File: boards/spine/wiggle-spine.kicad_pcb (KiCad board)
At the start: 2 copper layers, 114.3 x 88.9 mm, 187 parts, among them CON1 USB-B, CON2 XLR-3 Female, CON3 USB-A, CON4 2.5mm 5-24V 5A, CON5 5-24V 16A, CON6 PLR135, CON7 PLT133, Q1 DMN3190LDW, Q2 2N7002P, Q3 AOD4189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

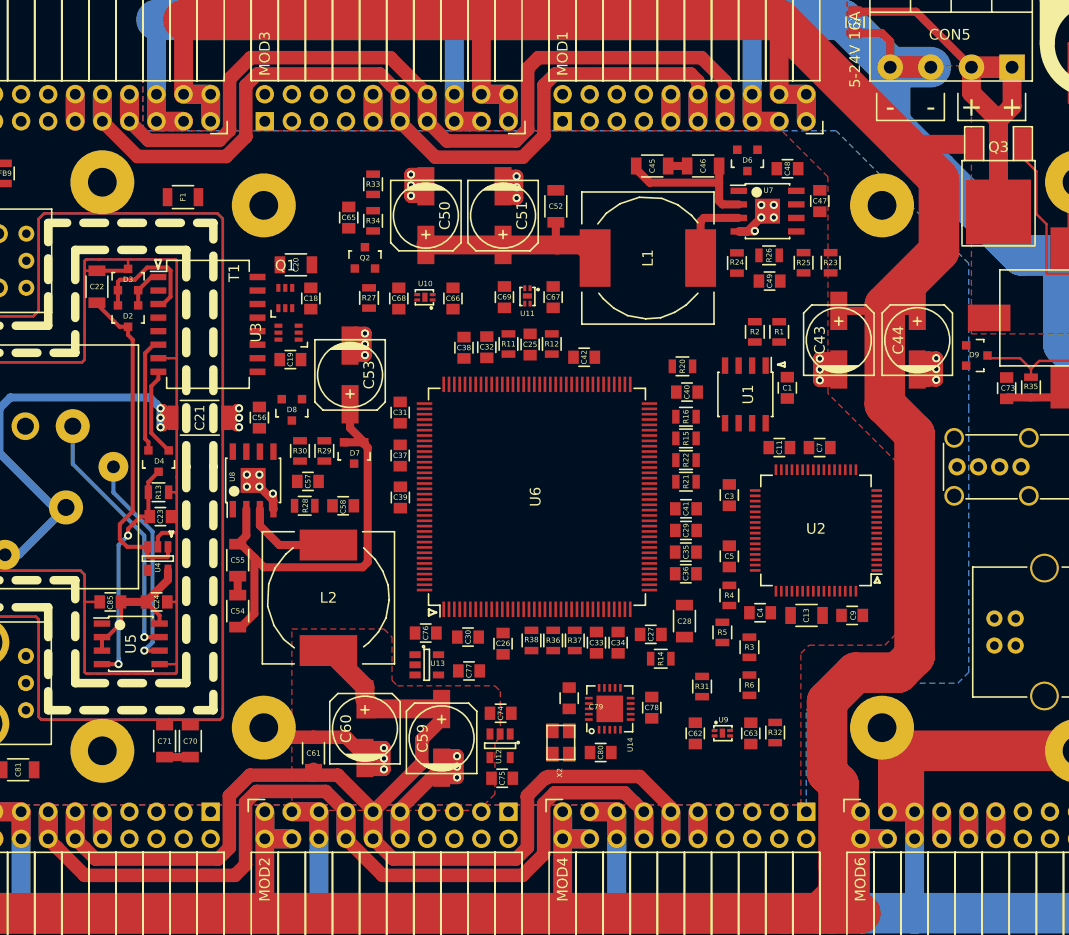
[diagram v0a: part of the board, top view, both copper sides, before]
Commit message: GND distribution, DMX via tweaks
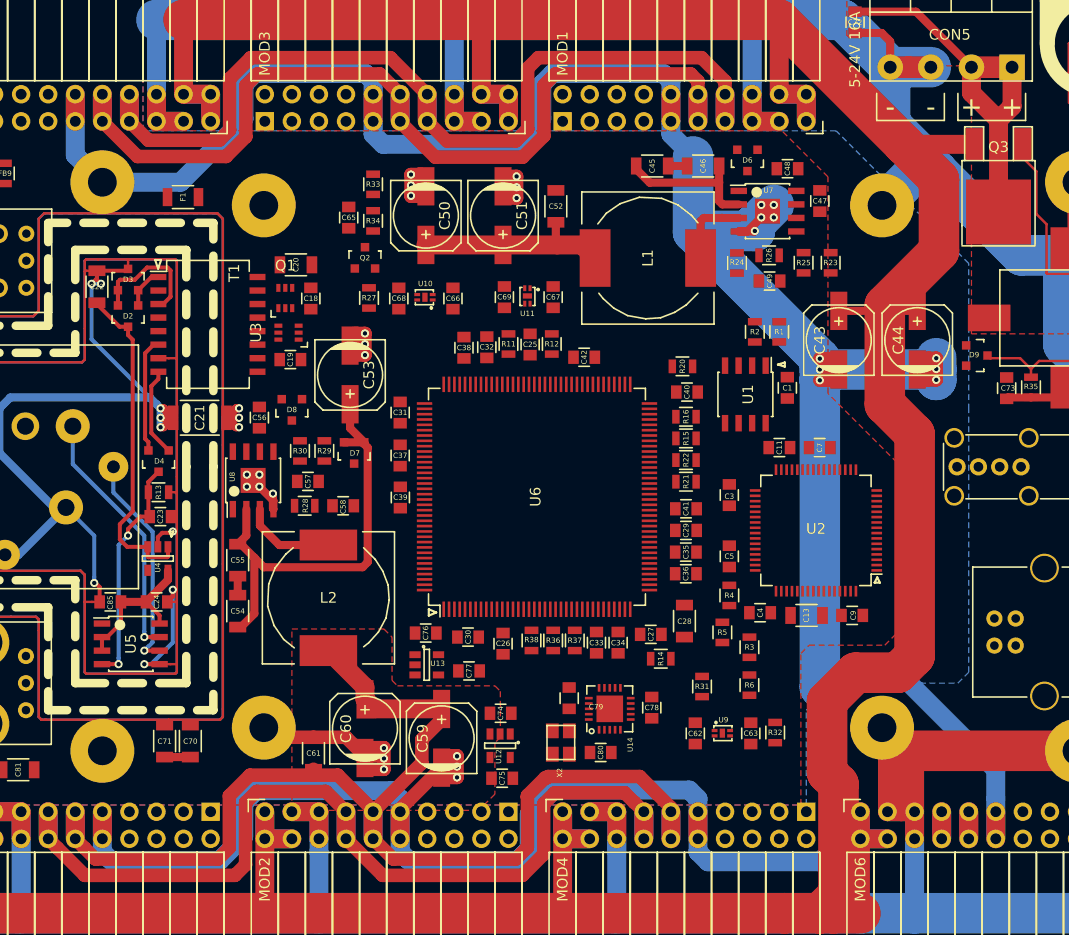
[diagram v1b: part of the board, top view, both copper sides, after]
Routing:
- net GND: track 365.1 -> 681.7 mm
- net /DMX512/DMXGND: track 269.8 -> 308.7 mm, vias 3 -> 9
- net GNDPWR: track 508.3 -> 514.8 mm

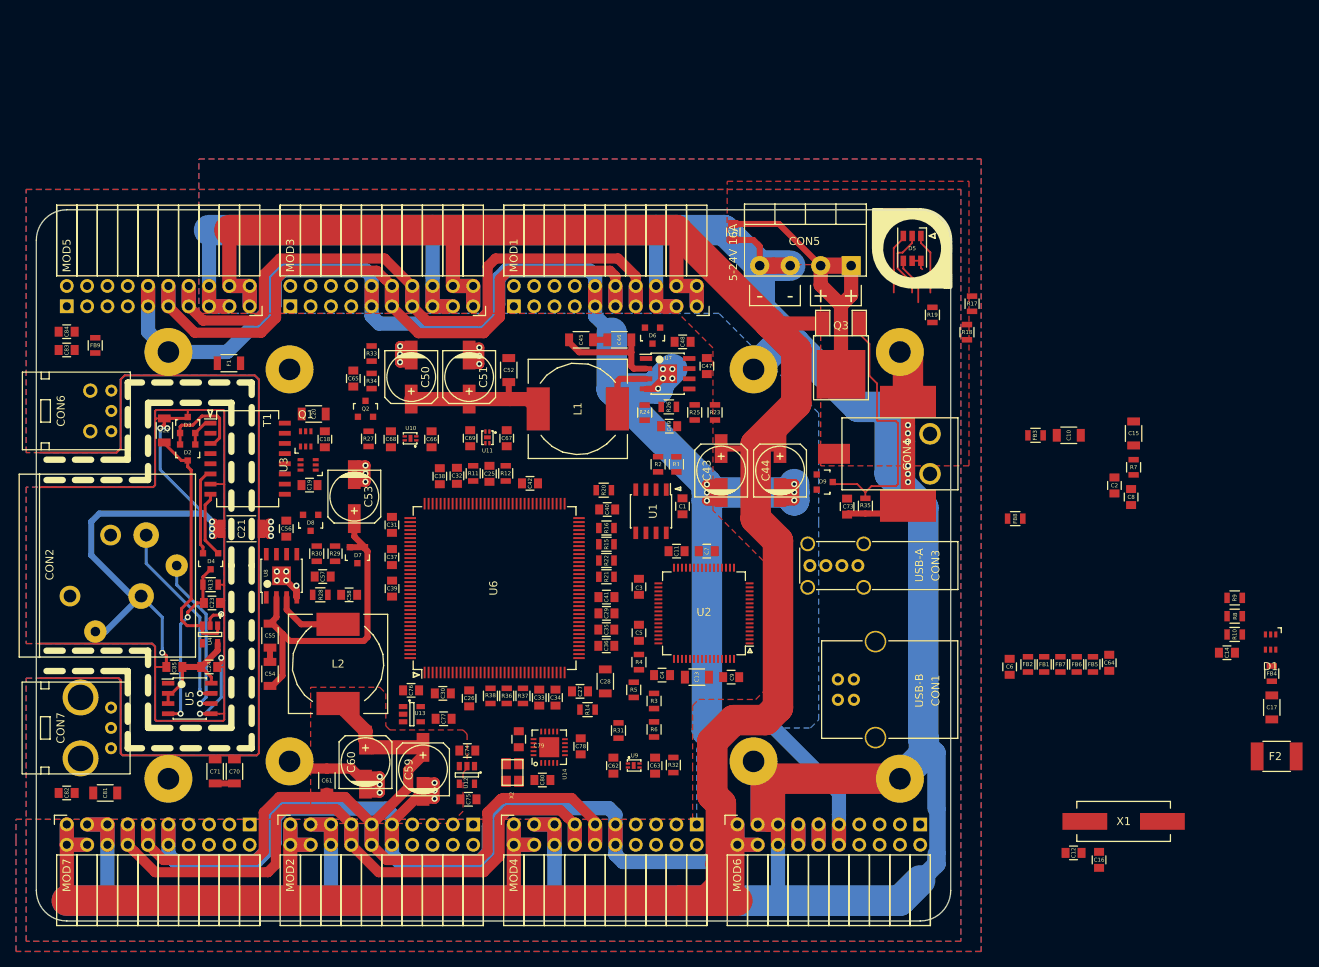
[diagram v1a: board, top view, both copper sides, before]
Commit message: Feeling better about GNDPWR and GND along the edges
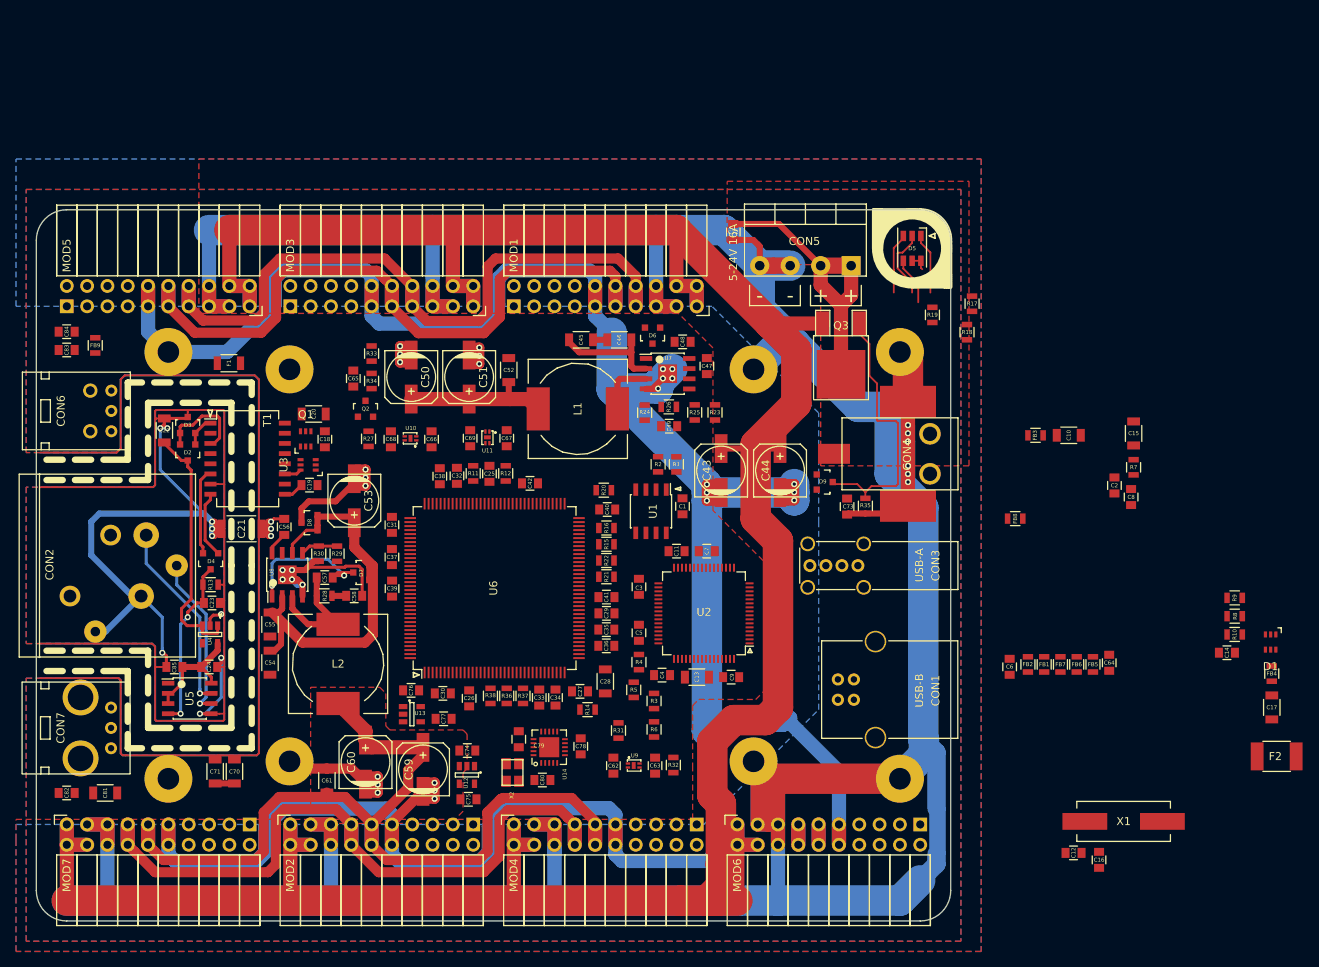
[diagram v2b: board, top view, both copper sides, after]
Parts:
- moved D7 2.21 mm to (125.7, 87.2), turned to 90 degrees
- moved C55 1.40 mm to (114.3, 93.8)
- moved C54 1.40 mm to (114.3, 98.5), turned to 270 degrees
- moved U8 0.73 mm to (116.5, 87.5)
- moved C58 0.65 mm to (124.8, 90.2)
- moved R28 0.52 mm to (121.1, 90.2)
- moved C53 0.51 mm to (124.8, 78.3)
- moved C56 0.34 mm to (116.1, 81.5), turned to 90 degrees
- moved C57 0.28 mm to (121.1, 87.9)
- moved R29 0.25 mm to (122.7, 84.9)
- moved R30 0.25 mm to (120.4, 84.9)
- moved D8 0.15 mm to (119.2, 81.0), turned to 90 degrees
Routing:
- net GND: track 681.7 -> 713.9 mm
- net Net-(C57-Pad2): track 0.00 -> 18.6 mm, vias 0 -> 2
- net +5V: track 228.3 -> 245.7 mm
- net Net-(C57-Pad1): track 8.72 -> 15.0 mm
- net Net-(R29-Pad1): track 0.00 -> 4.69 mm
- net Net-(C56-Pad1): track 0.00 -> 2.92 mm
- net Net-(C19-Pad1): track 0.00 -> 2.55 mm
- net Net-(T1-Pad11): track 0.00 -> 2.16 mm
- net Net-(C58-Pad2): track 0.00 -> 1.78 mm

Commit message: Wiggle through the thick verticals
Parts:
- moved R29 4.14 mm to (119.6, 82.2), turned to 180 degrees
- moved D7 3.61 mm to (122.9, 85.0)
- moved D8 1.89 mm to (119.3, 79.1), turned to 0 degrees
- moved C58 1.15 mm to (124.0, 89.4), turned to 270 degrees
- moved R27 0.95 mm to (126.6, 69.6), turned to 0 degrees
- moved R30 0.25 mm to (120.1, 84.9)
- moved R28 0.25 mm to (120.8, 90.2)
- moved U8 0.13 mm to (116.3, 87.5)
- moved C57 0.11 mm to (121.0, 87.9)
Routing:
- net +3V3: track 213.1 -> 332.6 mm
- net +5V: track 245.7 -> 292.5 mm
- net GND: track 713.9 -> 752.6 mm, vias 34 -> 37
- net Net-(C57-Pad2): track 18.6 -> 11.7 mm, vias 2 -> 1
- net GNDPWR: track 514.8 -> 509.8 mm

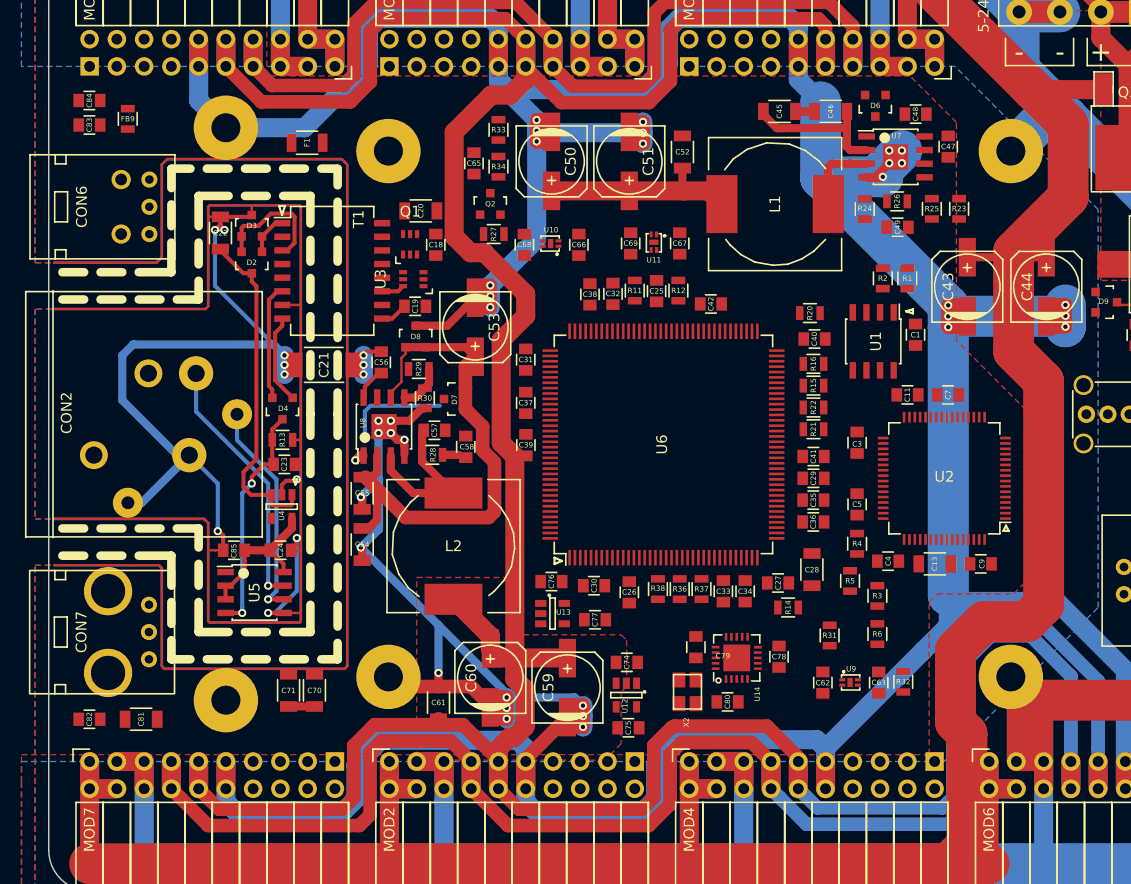
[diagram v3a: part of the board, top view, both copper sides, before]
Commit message: Lots more thick power routing
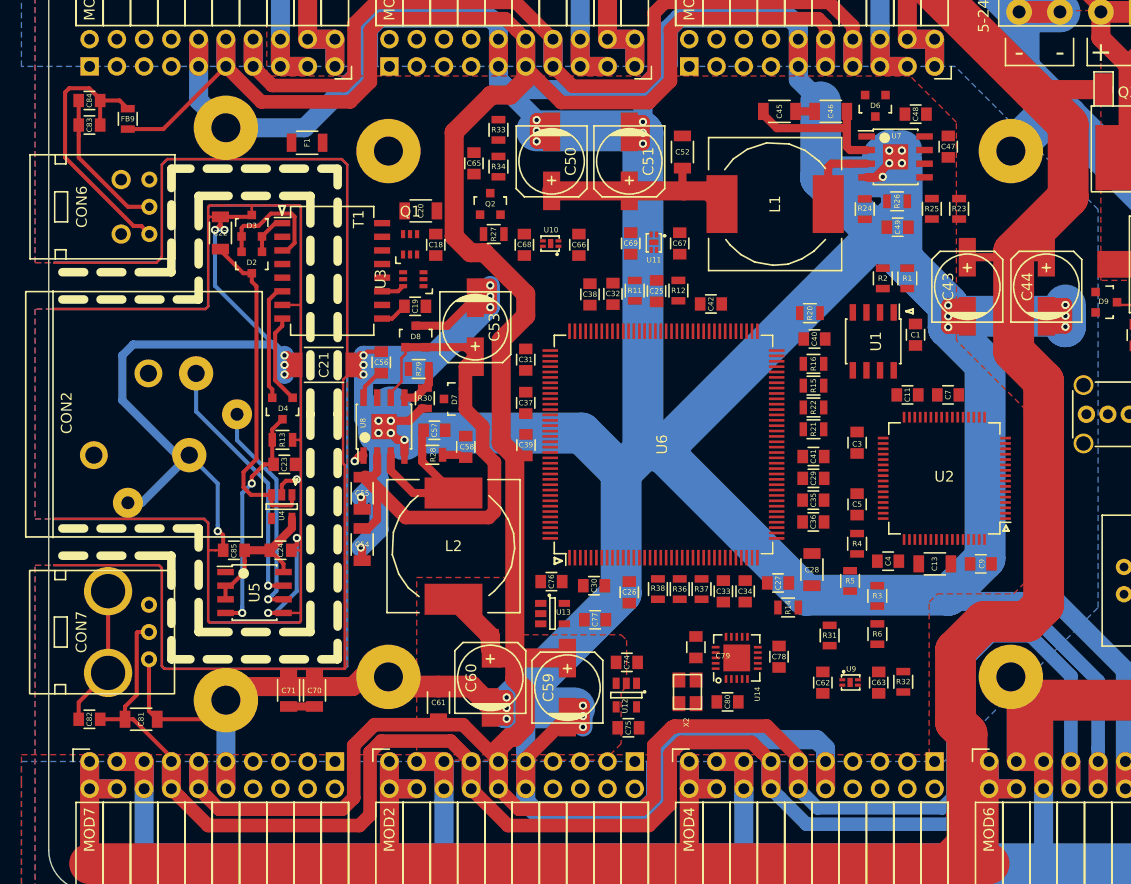
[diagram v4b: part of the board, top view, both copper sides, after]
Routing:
- net GND: track 752.6 -> 964.1 mm, vias 37 -> 36
- net Net-(C83-Pad2): track 0.00 -> 26.0 mm
- net +5V: track 292.5 -> 310.7 mm
- net +3V3: track 332.6 -> 343.6 mm
- net Net-(C57-Pad2): track 11.7 -> 1.22 mm

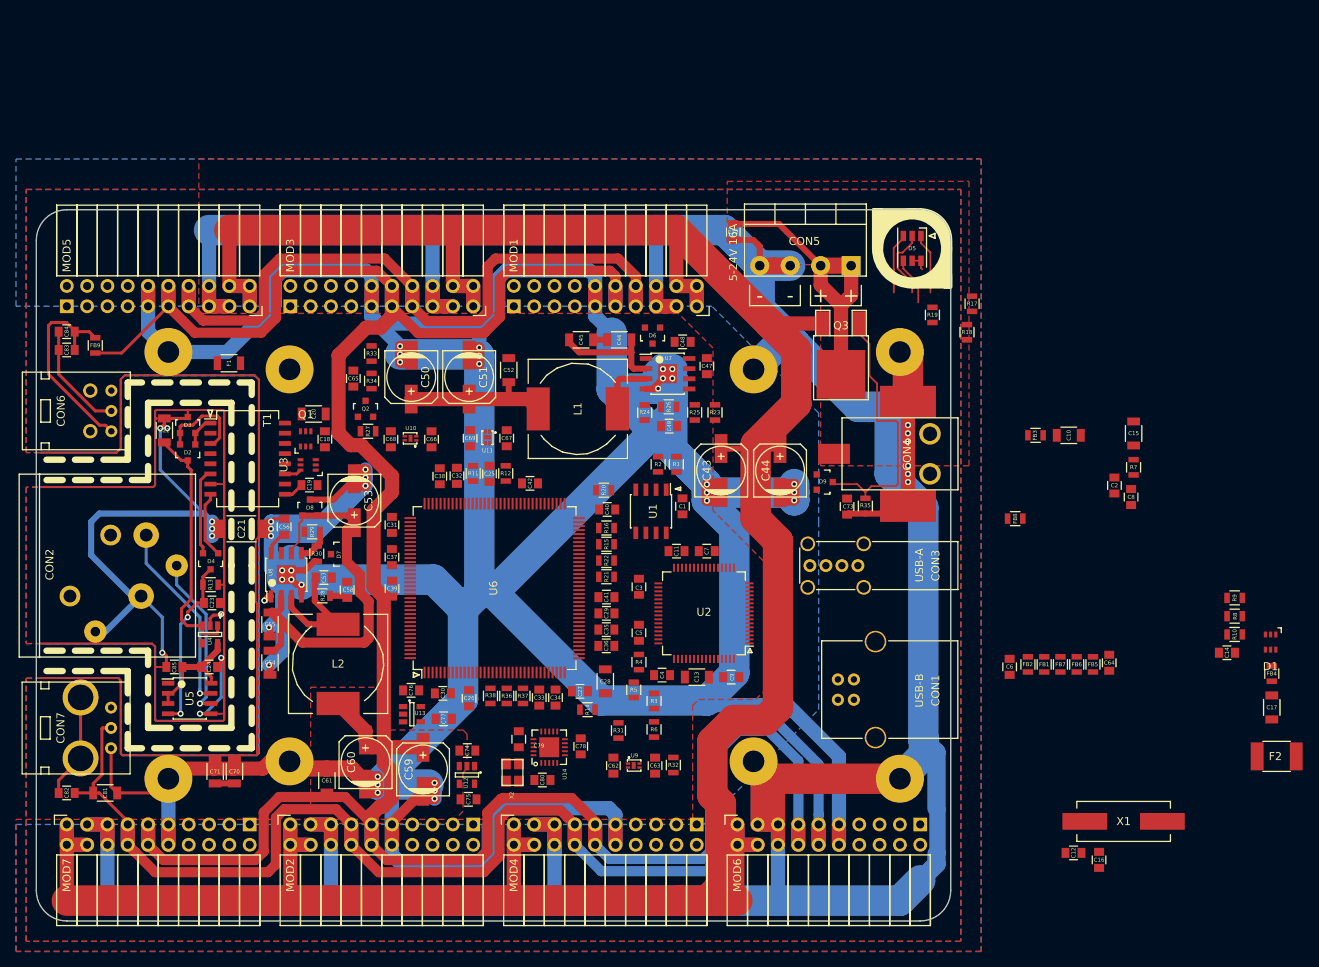
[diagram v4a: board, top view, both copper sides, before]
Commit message: More power routing, making room for the 5V vertical
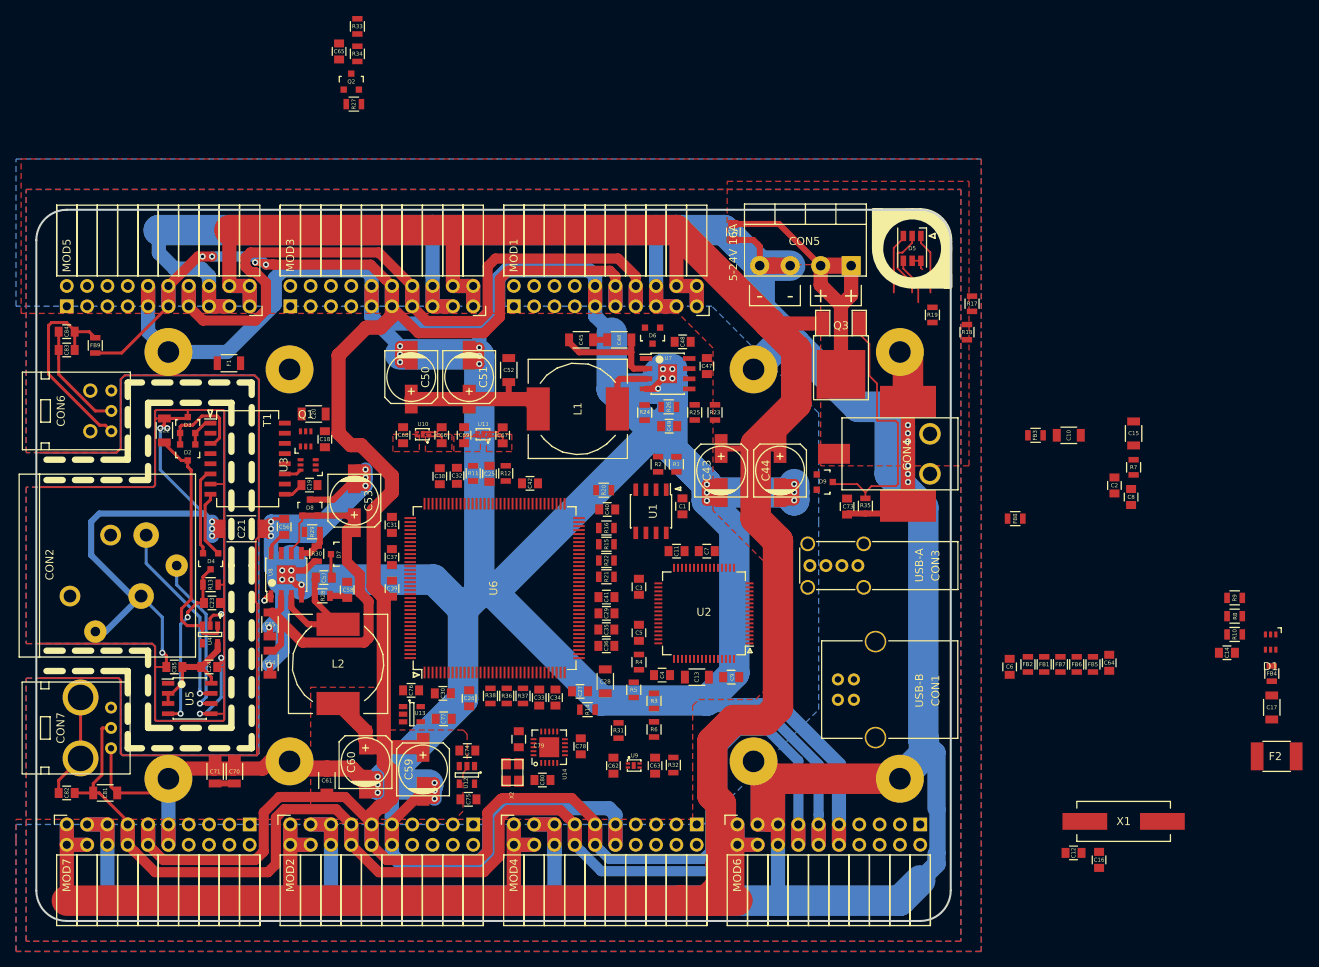
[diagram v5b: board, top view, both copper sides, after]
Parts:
- moved C65 40.9 mm to (122.9, 22.1)
- moved Q2 40.9 mm to (124.5, 25.9)
- moved R27 40.9 mm to (124.8, 28.7)
- moved R33 40.9 mm to (125.2, 19.0)
- moved R34 40.9 mm to (125.2, 22.4)
- moved C68 1.61 mm to (130.9, 70.1)
- moved U10 1.61 mm to (133.4, 70.0)
- moved C66 1.37 mm to (135.8, 70.1)
- moved C69 0.85 mm to (138.6, 70.1)
- moved U11 0.64 mm to (141.0, 70.0), turned to 90 degrees
- moved C67 0.63 mm to (143.4, 70.1), turned to 90 degrees
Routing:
- net GNDPWR: track 509.8 -> 520.7 mm
- net +5V: track 310.7 -> 318.8 mm
- net GND: track 964.1 -> 969.5 mm
- net Net-(C57-Pad2): track 1.22 -> 4.19 mm
- net +3V3: track 343.6 -> 346.3 mm, vias 0 -> 4
- net /Power/USB Power Output/5V_IN: track 18.6 -> 21.0 mm
- net /Power/VBUS_UPSTREAM: track 0.00 -> 2.44 mm
- added copper zone on F.Cu, net +5V
- added copper zone on F.Cu, net /Power/USB Power Output/5V_IN
- added copper zone on F.Cu, net /Power/VBUS_UPSTREAM

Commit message: Happy with the +5 vertical for now
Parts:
- moved C69 46.4 mm to (148.3, 24.7)
- moved C67 46.4 mm to (153.2, 24.8)
- moved U11 46.4 mm to (150.7, 24.6)
- moved C66 45.8 mm to (141.2, 24.6)
- moved C68 45.8 mm to (136.4, 24.6)
- moved U10 45.8 mm to (138.8, 24.5)
- moved C31 0.60 mm to (129.5, 81.9)
- moved C37 0.25 mm to (129.5, 85.6)
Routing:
- net +5V: track 318.8 -> 471.1 mm, vias 0 -> 1
- net +3V3: track 346.3 -> 339.7 mm
- net GND: track 969.5 -> 966.3 mm
